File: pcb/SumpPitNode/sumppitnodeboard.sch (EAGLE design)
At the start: 38 parts, among them IC1 7805T, J1 POWER_JACK

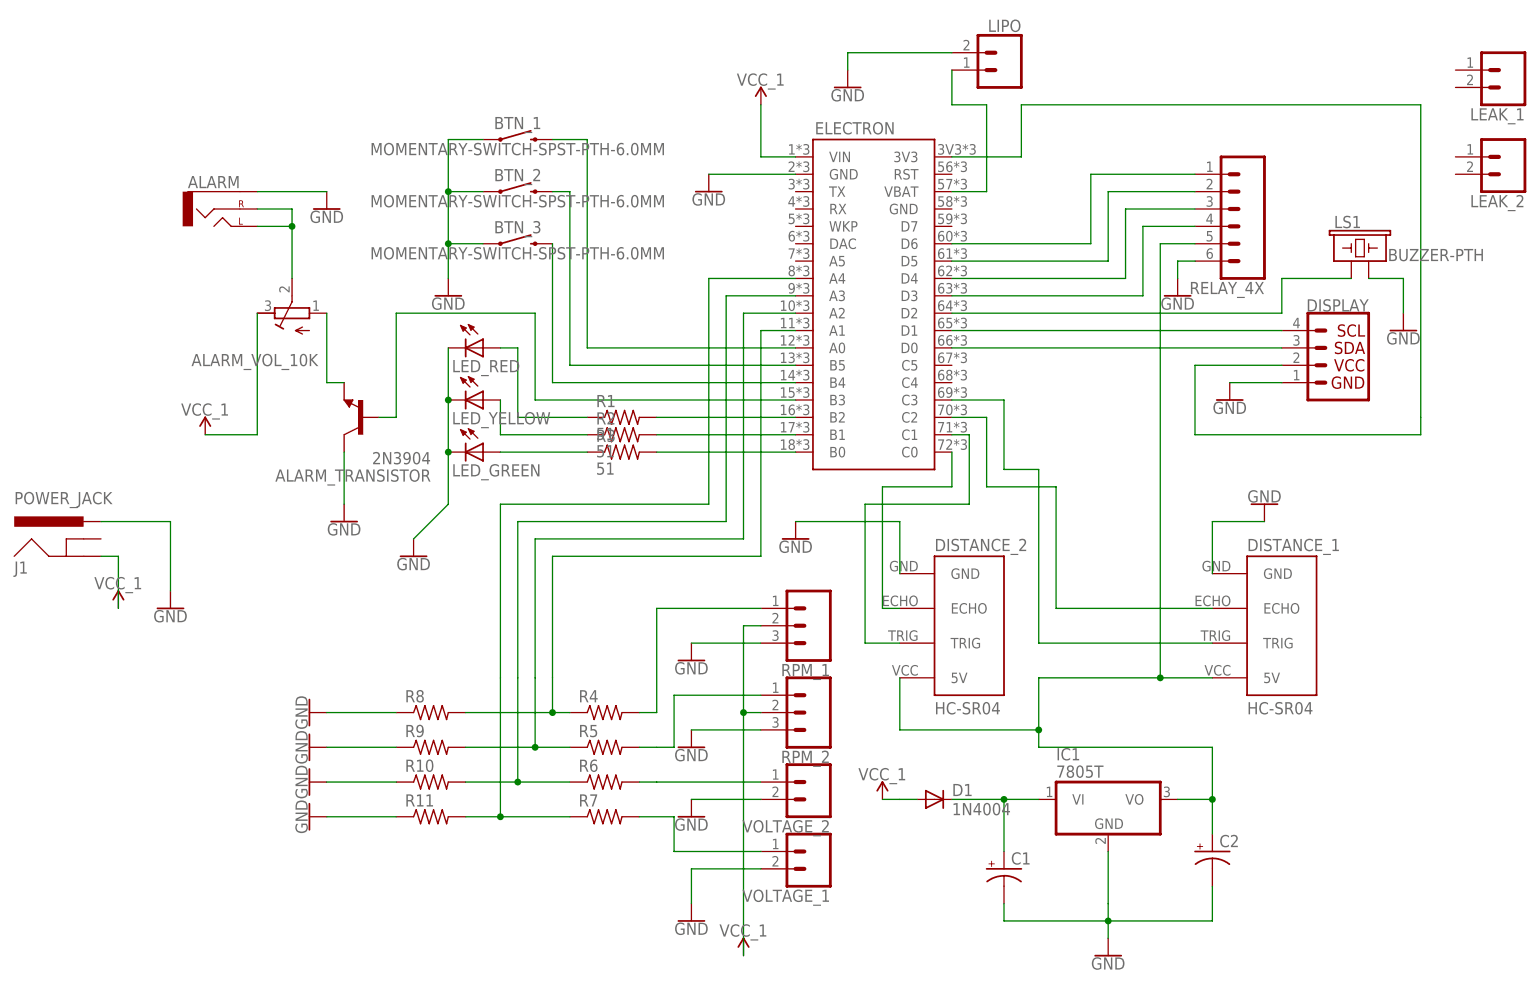
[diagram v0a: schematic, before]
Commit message: Connect leak sensors.
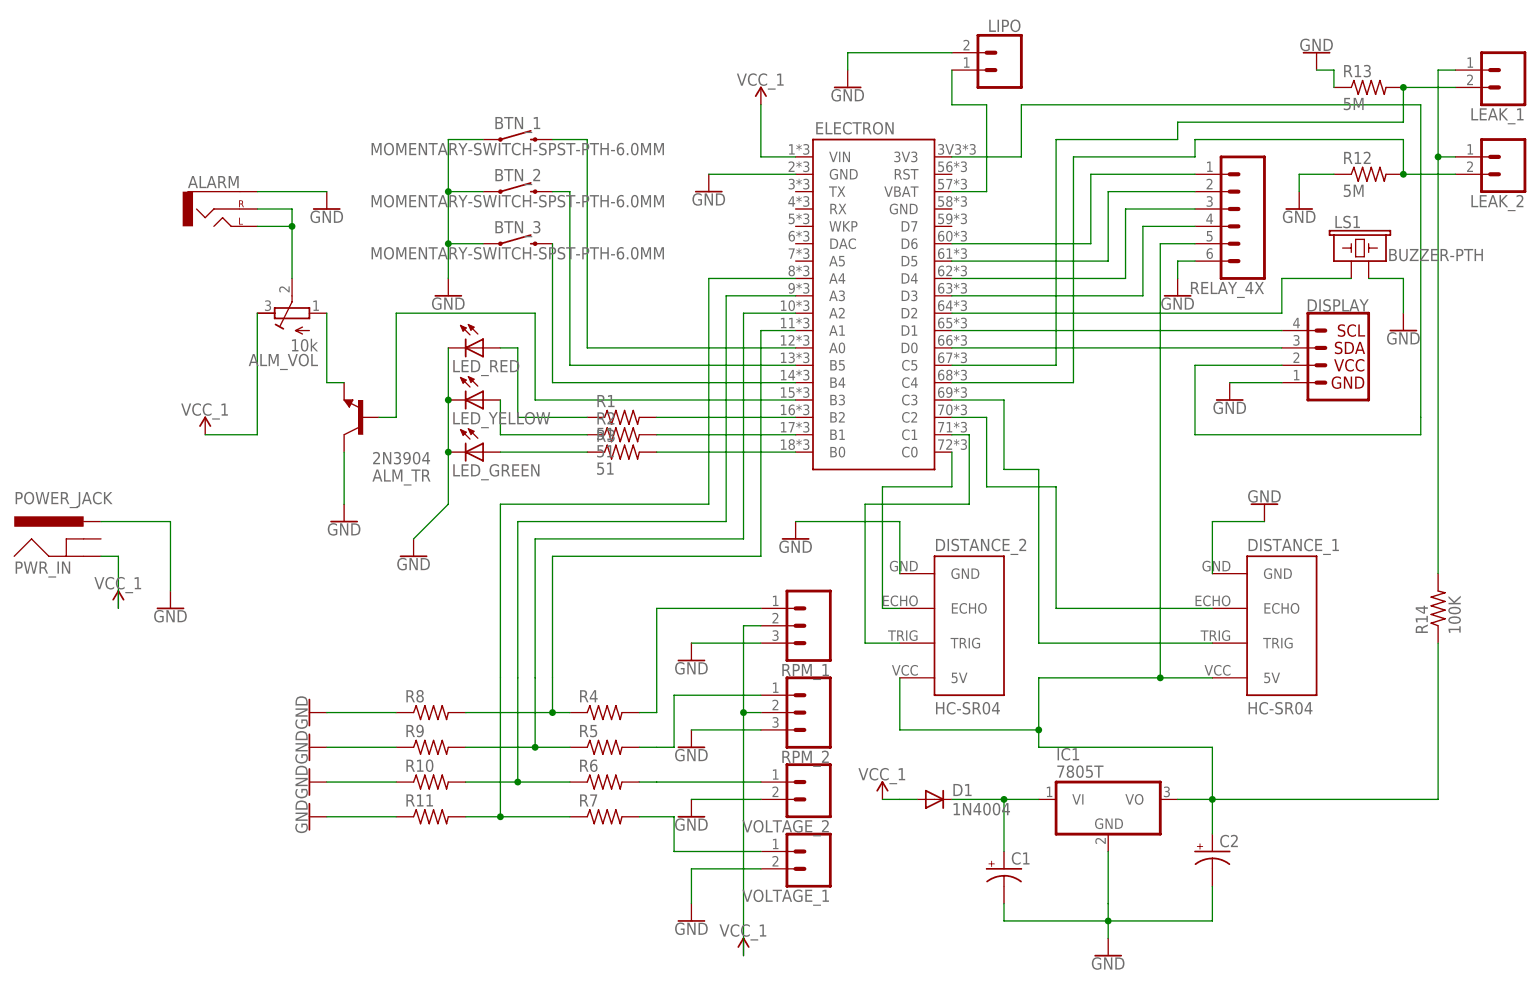
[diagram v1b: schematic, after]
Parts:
- added R12, R13: 5M, resistor:R-US_0204/5
- added R14: 100K, resistor:R-US_0204/5
- ALM_VOL: value (none) -> 10k
- renumbered ALARM_TRANSISTOR to ALM_TR, ALARM_VOL_10K to ALM_VOL, J1 to PWR_IN
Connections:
- new net N$23: ELECTRON.C5, LEAK_1.2, R13.2
- new net N$32: ELECTRON.C4, LEAK_2.2, R12.2
- new net N$38: LEAK_1.1, LEAK_2.1, R14.2
- net GND: now also R12.1, R13.1
- net N$33: now also R14.1
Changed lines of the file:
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@@
 <part name="BTN_3" library="SparkFun-Switches" library_urn="urn:adsk.eagle:library:535" deviceset="MOMENTARY-SWITCH-SPST" device="-PTH-6.0MM" package3d_urn="urn:adsk.eagle:package:40163/1"/>
 <part name="LIPO" library="SparkFun-Connectors" library_urn="urn:adsk.eagle:library:513" deviceset="CONN_02" device="JST-PTH-2" package3d_urn="urn:adsk.eagle:package:38053/1"/>
-<part name="ALARM_TRANSISTOR" library="transistor" library_urn="urn:adsk.eagle:library:402" deviceset="2N3904" device="" package3d_urn="urn:adsk.eagle:package:29893/2"/>
-<part name="ALARM_VOL_10K" library="rcl" library_urn="urn:adsk.eagle:library:334" deviceset="R-TRIMM" device="64W" package3d_urn="urn:adsk.eagle:package:23748/1"/>
+<part name="ALM_TR" library="transistor" library_urn="urn:adsk.eagle:library:402" deviceset="2N3904" device="" package3d_urn="urn:adsk.eagle:package:29893/2"/>
+<part name="ALM_VOL" library="rcl" library_urn="urn:adsk.eagle:library:334" deviceset="R-TRIMM" device="64W" package3d_urn="urn:adsk.eagle:package:23748/1" value="10k"/>
 <part name="VCC_12V" library="SparkFun-PowerSymbols" library_urn="urn:adsk.eagle:library:530" deviceset="VCC_1" device=""/>
 <part name="GND1" library="SparkFun-PowerSymbols" library_urn="urn:adsk.eagle:library:530" deviceset="GND" device=""/>
@@
 <part name="RELAY_4X" library="SparkFun-Connectors" deviceset="CONN_06" device="LOCK"/>
 <part name="GND20" library="SparkFun-PowerSymbols" library_urn="urn:adsk.eagle:library:530" deviceset="GND" device=""/>
-<part name="J1" library="SparkFun-Connectors" deviceset="POWER_JACK" device=""/>
+<part name="PWR_IN" library="SparkFun-Connectors" deviceset="POWER_JACK" device=""/>
 <part name="GND21" library="SparkFun-PowerSymbols" library_urn="urn:adsk.eagle:library:530" deviceset="GND" device=""/>
 <part name="VCC_12V4" library="SparkFun-PowerSymbols" library_urn="urn:adsk.eagle:library:530" deviceset="VCC_1" device=""/>
+<part name="R12" library="resistor" library_urn="urn:adsk.eagle:library:348" deviceset="R-US_" device="0204/5" package3d_urn="urn:adsk.eagle:package:25955/1" value="5M"/>
+<part name="R13" library="resistor" library_urn="urn:adsk.eagle:library:348" deviceset="R-US_" device="0204/5" package3d_urn="urn:adsk.eagle:package:25955/1" value="5M"/>
+<part name="GND22" library="SparkFun-PowerSymbols" library_urn="urn:adsk.eagle:library:530" deviceset="GND" device=""/>
+<part name="GND23" library="SparkFun-PowerSymbols" library_urn="urn:adsk.eagle:library:530" deviceset="GND" device=""/>
+<part name="R14" library="resistor" library_urn="urn:adsk.eagle:library:348" deviceset="R-US_" device="0204/5" package3d_urn="urn:adsk.eagle:package:25955/1" value="100K"/>
 </parts>
 <sheets>
@@
 <instance part="BTN_3" gate="G$1" x="-86.36" y="68.58"/>
 <instance part="LIPO" gate="G$1" x="-15.24" y="93.98" rot="MR0"/>
-<instance part="ALARM_TRANSISTOR" gate="G1" x="-109.22" y="43.18" rot="R180"/>
-<instance part="ALARM_VOL_10K" gate="G$1" x="-119.38" y="58.42" rot="R90"/>
+<instance part="ALM_TR" gate="G1" x="-109.22" y="43.18" rot="R180"/>
+<instance part="ALM_VOL" gate="G$1" x="-119.38" y="58.42" rot="R90"/>
 <instance part="VCC_12V" gate="G$2" x="-132.08" y="40.64"/>
 <instance part="GND1" gate="1" x="-114.3" y="73.66"/>
@@
 <instance part="RELAY_4X" gate="G$1" x="17.78" y="73.66" rot="R180"/>
 <instance part="GND20" gate="1" x="10.16" y="60.96"/>
-<instance part="J1" gate="G$1" x="-149.86" y="20.32"/>
+<instance part="PWR_IN" gate="G$1" x="-149.86" y="20.32"/>
 <instance part="GND21" gate="1" x="-137.16" y="15.24"/>
 <instance part="VCC_12V4" gate="G$2" x="-144.78" y="15.24"/>
+<instance part="R12" gate="G$1" x="38.1" y="78.74"/>
+<instance part="R13" gate="G$1" x="38.1" y="91.44"/>
+<instance part="GND22" gate="1" x="30.48" y="96.52" rot="R180"/>
+<instance part="GND23" gate="1" x="27.94" y="73.66"/>
+<instance part="R14" gate="G$1" x="48.26" y="15.24" rot="R90"/>
 </instances>
 <busses>
@@
 <net name="N$1" class="0">
 <segment>
-<pinref part="ALARM_VOL_10K" gate="G$1" pin="S"/>
+<pinref part="ALM_VOL" gate="G$1" pin="S"/>
 <pinref part="ALARM" gate="G$1" pin="RIGHT"/>
 <wire x1="-119.38" y1="63.5" x2="-119.38" y2="71.12" width="0.1524" layer="91"/>
@@
 </segment>
 <segment>
-<pinref part="ALARM_TRANSISTOR" gate="G1" pin="C"/>
+<pinref part="ALM_TR" gate="G1" pin="C"/>
 <pinref part="GND2" gate="1" pin="GND"/>
 <wire x1="-111.76" y1="30.48" x2="-111.76" y2="38.1" width="0.1524" layer="91"/>
@@
 <pinref part="GND21" gate="1" pin="GND"/>
 <wire x1="-137.16" y1="17.78" x2="-137.16" y2="27.94" width="0.1524" layer="91"/>
-<pinref part="J1" gate="G$1" pin="PWR"/>
+<pinref part="PWR_IN" gate="G$1" pin="PWR"/>
 <wire x1="-137.16" y1="27.94" x2="-147.32" y2="27.94" width="0.1524" layer="91"/>
 </segment>
+<segment>
+<pinref part="GND23" gate="1" pin="GND"/>
+<pinref part="R12" gate="G$1" pin="1"/>
+<wire x1="27.94" y1="76.2" x2="27.94" y2="78.74" width="0.1524" layer="91"/>
+<wire x1="27.94" y1="78.74" x2="33.02" y2="78.74" width="0.1524" layer="91"/>
+</segment>
+<segment>
+<pinref part="R13" gate="G$1" pin="1"/>
+<pinref part="GND22" gate="1" pin="GND"/>
+<wire x1="33.02" y1="91.44" x2="33.02" y2="93.98" width="0.1524" layer="91"/>
+<wire x1="33.02" y1="93.98" x2="30.48" y2="93.98" width="0.1524" layer="91"/>
+</segment>
 </net>
 <net name="N$2" class="0">
 <segment>
-<pinref part="ALARM_VOL_10K" gate="G$1" pin="A"/>
-<pinref part="ALARM_TRANSISTOR" gate="G1" pin="E"/>
+<pinref part="ALM_VOL" gate="G$1" pin="A"/>
+<pinref part="ALM_TR" gate="G1" pin="E"/>
 <wire x1="-114.3" y1="58.42" x2="-114.3" y2="48.26" width="0.1524" layer="91"/>
 <wire x1="-114.3" y1="48.26" x2="-111.76" y2="48.26" width="0.1524" layer="91"/>
@@
 <wire x1="-83.82" y1="58.42" x2="-104.14" y2="58.42" width="0.1524" layer="91"/>
 <wire x1="-104.14" y1="58.42" x2="-104.14" y2="43.18" width="0.1524" layer="91"/>
-<pinref part="ALARM_TRANSISTOR" gate="G1" pin="B"/>
+<pinref part="ALM_TR" gate="G1" pin="B"/>
 <wire x1="-104.14" y1="43.18" x2="-106.68" y2="43.18" width="0.1524" layer="91"/>
 </segment>
@@
 <wire x1="-124.46" y1="58.42" x2="-124.46" y2="40.64" width="0.1524" layer="91"/>
 <wire x1="-124.46" y1="40.64" x2="-132.08" y2="40.64" width="0.1524" layer="91"/>
-<pinref part="ALARM_VOL_10K" gate="G$1" pin="E"/>
+<pinref part="ALM_VOL" gate="G$1" pin="E"/>
 </segment>
 <segment>
 <pinref part="VCC_12V4" gate="G$2" pin="VCC_1"/>
 <wire x1="-144.78" y1="15.24" x2="-144.78" y2="22.86" width="0.1524" layer="91"/>
-<pinref part="J1" gate="G$1" pin="GND"/>
+<pinref part="PWR_IN" gate="G$1" pin="GND"/>
 <wire x1="-144.78" y1="22.86" x2="-147.32" y2="22.86" width="0.1524" layer="91"/>
 </segment>
@@
 <wire x1="7.62" y1="68.58" x2="7.62" y2="5.08" width="0.1524" layer="91"/>
 <junction x="7.62" y="5.08"/>
+<wire x1="15.24" y1="-12.7" x2="48.26" y2="-12.7" width="0.1524" layer="91"/>
+<wire x1="48.26" y1="-12.7" x2="48.26" y2="10.16" width="0.1524" layer="91"/>
+<pinref part="R14" gate="G$1" pin="1"/>
 </segment>
 </net>
@@
 </segment>
 </net>
+<net name="N$23" class="0">
+<segment>
+<pinref part="LEAK_1" gate="G$1" pin="2"/>
+<pinref part="R13" gate="G$1" pin="2"/>
+<wire x1="50.8" y1="91.44" x2="43.18" y2="91.44" width="0.1524" layer="91"/>
+<wire x1="43.18" y1="91.44" x2="43.18" y2="86.36" width="0.1524" layer="91"/>
+<junction x="43.18" y="91.44"/>
+<wire x1="43.18" y1="86.36" x2="10.16" y2="86.36" width="0.1524" layer="91"/>
+<wire x1="10.16" y1="86.36" x2="10.16" y2="83.82" width="0.1524" layer="91"/>
+<wire x1="10.16" y1="83.82" x2="-7.62" y2="83.82" width="0.1524" layer="91"/>
+<wire x1="-7.62" y1="83.82" x2="-7.62" y2="50.8" width="0.1524" layer="91"/>
+<pinref part="ELECTRON" gate="G$1" pin="C5"/>
+<wire x1="-7.62" y1="50.8" x2="-22.86" y2="50.8" width="0.1524" layer="91"/>
+</segment>
+</net>
+<net name="N$32" class="0">
+<segment>
+<pinref part="LEAK_2" gate="G$1" pin="2"/>
+<pinref part="R12" gate="G$1" pin="2"/>
+<wire x1="50.8" y1="78.74" x2="43.18" y2="78.74" width="0.1524" layer="91"/>
+<wire x1="43.18" y1="78.74" x2="43.18" y2="83.82" width="0.1524" layer="91"/>
+<junction x="43.18" y="78.74"/>
+<wire x1="43.18" y1="83.82" x2="12.7" y2="83.82" width="0.1524" layer="91"/>
+<wire x1="12.7" y1="83.82" x2="12.7" y2="81.28" width="0.1524" layer="91"/>
+<wire x1="12.7" y1="81.28" x2="-5.08" y2="81.28" width="0.1524" layer="91"/>
+<wire x1="-5.08" y1="81.28" x2="-5.08" y2="48.26" width="0.1524" layer="91"/>
+<pinref part="ELECTRON" gate="G$1" pin="C4"/>
+<wire x1="-5.08" y1="48.26" x2="-22.86" y2="48.26" width="0.1524" layer="91"/>
+</segment>
+</net>
+<net name="N$38" class="0">
+<segment>
+<pinref part="LEAK_1" gate="G$1" pin="1"/>
+<wire x1="48.26" y1="93.98" x2="50.8" y2="93.98" width="0.1524" layer="91"/>
+<pinref part="LEAK_2" gate="G$1" pin="1"/>
+<wire x1="48.26" y1="81.28" x2="50.8" y2="81.28" width="0.1524" layer="91"/>
+<wire x1="48.26" y1="81.28" x2="48.26" y2="93.98" width="0.1524" layer="91"/>
+<junction x="48.26" y="81.28"/>
+<wire x1="48.26" y1="20.32" x2="48.26" y2="81.28" width="0.1524" layer="91"/>
+<pinref part="R14" gate="G$1" pin="2"/>
+</segment>
+</net>
